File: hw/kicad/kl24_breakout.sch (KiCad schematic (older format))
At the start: 21 parts

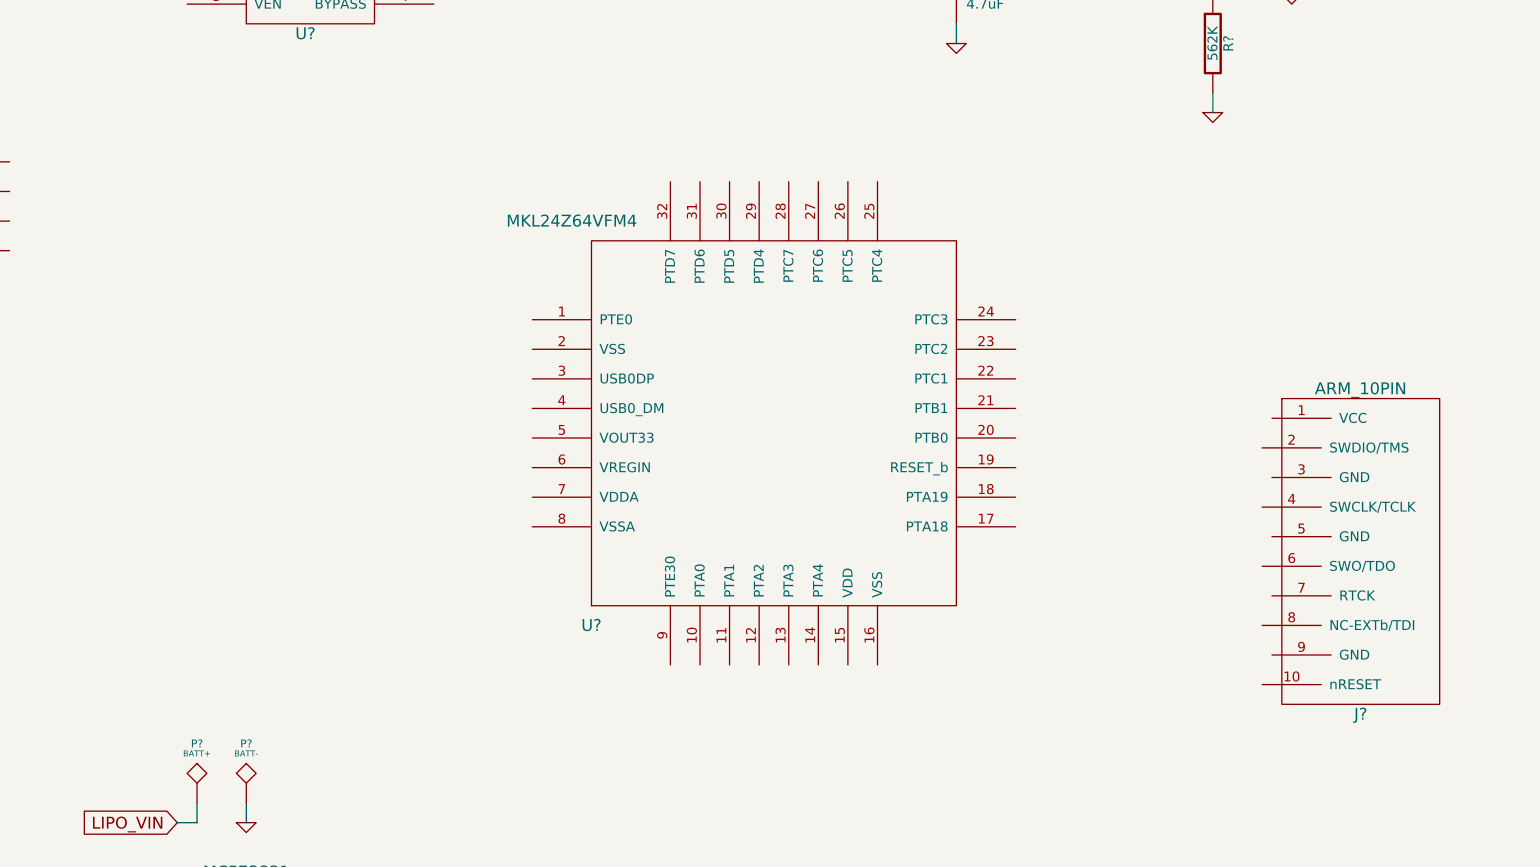
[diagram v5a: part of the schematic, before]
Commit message: - add some usb things and a crystal+load caps
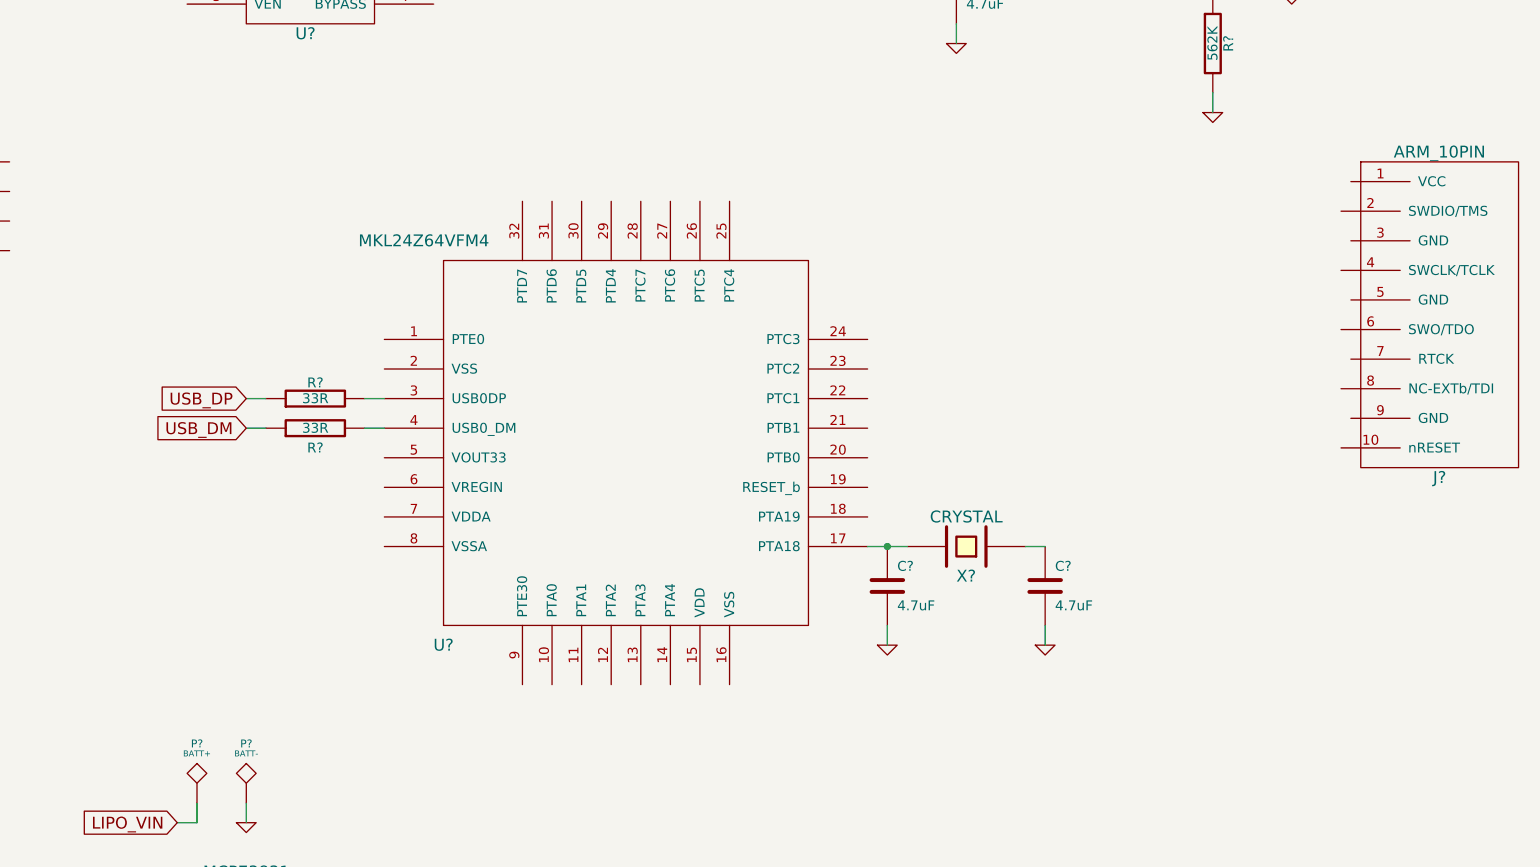
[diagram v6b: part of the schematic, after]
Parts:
- added C? (x2): 4.7uF, symbol C
- added R? (x2): 33R, symbol R
- added X?: CRYSTAL, ~, symbol CRYSTAL
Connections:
- net GND: now also C?.2, C?.2
- net USB_DM: now also R?.1
- net USB_DP: now also R?.1
- net at U?.17 (PTA18): now also C?.1, X?.2
- net at U?.3 (USB0DP): now also R?.2
- net at U?.4 (USB0_DM): now also R?.2
- new net: C?.1, X?.1
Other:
- moved on the sheet: J?, U?
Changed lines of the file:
@@
-EESchema Schematic File Version 2  date 3/9/2013 12:31:52 PM
+EESchema Schematic File Version 2  date 3/9/2013 4:44:26 PM
 LIBS:power
 LIBS:device
@@
 LIBS:kl24_breakout
 LIBS:kl24_breakout-cache
-EELAYER 25  0
+EELAYER 27 0
 EELAYER END
-$Descr A4 11700 8267
+$Descr A4 11693 8268
 encoding utf-8
 Sheet 1 1
@@
 F 0 "#PWR?" H 5700 6950 30  0001 C CNN
 F 1 "GND" H 5700 6880 30  0001 C CNN
+F 2 "" H 5700 6950 60  0001 C CNN
+F 3 "" H 5700 6950 60  0001 C CNN
 	1    5700 6950
 	1    0    0    -1
@@
 F 0 "C?" H 5750 6750 50  0000 L CNN
 F 1 "4.7uF" H 5750 6550 50  0000 L CNN
+F 2 "" H 5700 6650 60  0001 C CNN
+F 3 "" H 5700 6650 60  0001 C CNN
 	1    5700 6650
 	1    0    0    -1
@@
 F 0 "R?" V 5530 6850 50  0000 C CNN
 F 1 "2K" V 5450 6850 50  0000 C CNN
+F 2 "" H 5450 6850 60  0001 C CNN
+F 3 "" H 5450 6850 60  0001 C CNN
 	1    5450 6850
 	1    0    0    -1
@@
 F 0 "R?" V 3780 7200 50  0000 C CNN
 F 1 "470R" V 3700 7200 50  0000 C CNN
+F 2 "" H 3700 7200 60  0001 C CNN
+F 3 "" H 3700 7200 60  0001 C CNN
 	1    3700 7200
 	1    0    0    -1
@@
 F 0 "D?" H 3700 6750 50  0000 C CNN
 F 1 "LED" H 3700 6550 50  0000 C CNN
+F 2 "" H 3700 6650 60  0001 C CNN
+F 3 "" H 3700 6650 60  0001 C CNN
 	1    3700 6650
 	0    1    1    0
@@
 F 0 "#PWR?" H 3300 6950 30  0001 C CNN
 F 1 "GND" H 3300 6880 30  0001 C CNN
+F 2 "" H 3300 6950 60  0001 C CNN
+F 3 "" H 3300 6950 60  0001 C CNN
 	1    3300 6950
 	1    0    0    -1
@@
 F 0 "C?" H 3200 6750 50  0000 L CNN
 F 1 "4.7uF" H 3100 6550 50  0000 L CNN
+F 2 "" H 3300 6650 60  0001 C CNN
+F 3 "" H 3300 6650 60  0001 C CNN
 	1    3300 6650
 	1    0    0    -1
@@
 F 0 "#PWR?" H 5150 6850 30  0001 C CNN
 F 1 "GND" H 5150 6780 30  0001 C CNN
+F 2 "" H 5150 6850 60  0001 C CNN
+F 3 "" H 5150 6850 60  0001 C CNN
 	1    5150 6850
 	1    0    0    -1
@@
 F 0 "L?" V 7750 1200 40  0000 C CNN
 F 1 "INDUCTOR" V 7900 1200 40  0000 C CNN
+F 2 "" H 7800 1200 60  0001 C CNN
+F 3 "" H 7800 1200 60  0001 C CNN
 	1    7800 1200
 	0    -1   -1   0
@@
 F 0 "#PWR?" H 9800 1850 30  0001 C CNN
 F 1 "GND" H 9800 1780 30  0001 C CNN
+F 2 "" H 9800 1850 60  0001 C CNN
+F 3 "" H 9800 1850 60  0001 C CNN
 	1    9800 1850
 	1    0    0    -1
@@
 F 0 "C?" H 9850 1650 50  0000 L CNN
 F 1 "10uF" H 9850 1450 50  0000 L CNN
+F 2 "" H 9800 1550 60  0001 C CNN
+F 3 "" H 9800 1550 60  0001 C CNN
 	1    9800 1550
 	1    0    0    -1
@@
 F 0 "#PWR?" H 9400 2450 30  0001 C CNN
 F 1 "GND" H 9400 2380 30  0001 C CNN
+F 2 "" H 9400 2450 60  0001 C CNN
+F 3 "" H 9400 2450 60  0001 C CNN
 	1    9400 2450
 	1    0    0    -1
@@
 F 0 "R?" V 9480 2100 50  0000 C CNN
 F 1 "562K" V 9400 2100 50  0000 C CNN
+F 2 "" H 9400 2100 60  0001 C CNN
+F 3 "" H 9400 2100 60  0001 C CNN
 	1    9400 2100
 	1    0    0    -1
@@
 F 0 "R?" V 9630 1600 50  0000 C CNN
 F 1 "976K" V 9550 1600 50  0000 C CNN
+F 2 "" H 9550 1600 60  0001 C CNN
+F 3 "" H 9550 1600 60  0001 C CNN
 	1    9550 1600
 	1    0    0    -1
@@
 F 0 "#PWR?" H 8100 1350 30  0001 C CNN
 F 1 "GND" H 8100 1280 30  0001 C CNN
+F 2 "" H 8100 1350 60  0001 C CNN
+F 3 "" H 8100 1350 60  0001 C CNN
 	1    8100 1350
 	1    0    0    -1
@@
 F 0 "#PWR?" H 8100 2100 30  0001 C CNN
 F 1 "GND" H 8100 2030 30  0001 C CNN
+F 2 "" H 8100 2100 60  0001 C CNN
+F 3 "" H 8100 2100 60  0001 C CNN
 	1    8100 2100
 	1    0    0    -1
@@
 F 0 "C?" H 8150 1900 50  0000 L CNN
 F 1 "4.7uF" H 8150 1700 50  0000 L CNN
+F 2 "" H 8100 1800 60  0001 C CNN
+F 3 "" H 8100 1800 60  0001 C CNN
 	1    8100 1800
 	1    0    0    -1
@@
 F 0 "#PWR?" H 2350 5450 30  0001 C CNN
 F 1 "GND" H 2350 5380 30  0001 C CNN
+F 2 "" H 2350 5450 60  0001 C CNN
+F 3 "" H 2350 5450 60  0001 C CNN
 	1    2350 5450
 	1    0    0    -1
@@
 F 0 "#PWR?" H 4500 6050 30  0001 C CNN
 F 1 "GND" H 4500 5980 30  0001 C CNN
+F 2 "" H 4500 6050 60  0001 C CNN
+F 3 "" H 4500 6050 60  0001 C CNN
 	1    4500 6050
 	1    0    0    -1
@@
 F 0 "#PWR?" H 9800 950 30  0001 C CNN
 F 1 "GND" H 9800 880 30  0001 C CNN
+F 2 "" H 9800 950 60  0001 C CNN
+F 3 "" H 9800 950 60  0001 C CNN
 	1    9800 950
 	1    0    0    -1
@@
 F 0 "P?" H 9800 1150 40  0000 C CNN
 F 1 "BATT_BACKUP-" H 9800 1100 30  0000 C CNN
+F 2 "" H 9800 850 60  0001 C CNN
+F 3 "" H 9800 850 60  0001 C CNN
 	1    9800 850
 	1    0    0    -1
@@
 F 0 "P?" H 9400 1400 40  0000 C CNN
 F 1 "BATT_BACKUP+" H 9400 1350 30  0000 C CNN
+F 2 "" H 9400 1100 60  0001 C CNN
+F 3 "" H 9400 1100 60  0001 C CNN
 	1    9400 1100
 	1    0    0    -1
@@
 F 0 "U?" H 8750 1050 60  0000 C CNN
 F 1 "MCP1640_SOT23" H 8750 1650 60  0000 C CNN
+F 2 "" H 8750 1350 60  0001 C CNN
+F 3 "" H 8750 1350 60  0001 C CNN
 	1    8750 1350
 	1    0    0    -1
@@
 F 0 "U?" H 4500 6300 60  0000 C CNN
 F 1 "MCP73831" H 4500 6900 60  0000 C CNN
+F 2 "" H 4500 6600 60  0001 C CNN
+F 3 "" H 4500 6600 60  0001 C CNN
 	1    4500 6600
 	1    0    0    -1
@@
 F 0 "U?" H 2600 2600 60  0000 C CNN
 F 1 "MCP1252-33X50I" H 2600 3350 60  0000 C CNN
+F 2 "" H 2600 2950 60  0001 C CNN
+F 3 "" H 2600 2950 60  0001 C CNN
 	1    2600 2950
 	1    0    0    -1
@@
 F 0 "U?" H 4800 1450 60  0000 C CNN
 F 1 "LP3985" H 4850 2050 60  0000 C CNN
+F 2 "" H 4800 1750 60  0001 C CNN
+F 3 "" H 4800 1750 60  0001 C CNN
 	1    4800 1750
 	1    0    0    -1
@@
 L ARM_10PIN J?
 U 1 1 51353F09
-P 10150 4500
-F 0 "J?" H 10150 3500 60  0000 C CNN
-F 1 "ARM_10PIN" H 10150 5150 60  0000 C CNN
-	1    10150 4500
+P 10550 3300
+F 0 "J?" H 10550 2300 60  0000 C CNN
+F 1 "ARM_10PIN" H 10550 3950 60  0000 C CNN
+F 2 "" H 10550 3300 60  0001 C CNN
+F 3 "" H 10550 3300 60  0001 C CNN
+	1    10550 3300
 	-1   0    0    -1
 $EndComp
@@
 F 0 "P?" H 4500 6250 40  0000 C CNN
 F 1 "BATT-" H 4500 6200 30  0000 C CNN
+F 2 "" H 4500 5950 60  0001 C CNN
+F 3 "" H 4500 5950 60  0001 C CNN
 	1    4500 5950
 	1    0    0    -1
@@
 F 0 "P?" H 4250 6250 40  0000 C CNN
 F 1 "BATT+" H 4250 6200 30  0000 C CNN
+F 2 "" H 4250 5950 60  0001 C CNN
+F 3 "" H 4250 5950 60  0001 C CNN
 	1    4250 5950
 	1    0    0    -1
@@
 F 0 "J?" H 1950 4400 60  0000 C CNN
 F 1 "USB-micro-ab" H 1950 5650 60  0000 C CNN
+F 2 "" H 1950 5000 60  0001 C CNN
+F 3 "" H 1950 5000 60  0001 C CNN
 	1    1950 5000
 	1    0    0    -1
@@
 L MKL24Z64VFM4 U?
 U 1 1 512F925B
-P 6650 4400
-F 0 "U?" H 6250 3750 60  0000 C CNN
-F 1 "MKL24Z64VFM4" H 6150 5800 60  0000 C CNN
-	1    6650 4400
-	1    0    0    -1
-$EndComp
+P 5900 4500
+F 0 "U?" H 5500 3850 60  0000 C CNN
+F 1 "MKL24Z64VFM4" H 5400 5900 60  0000 C CNN
+F 2 "" H 5900 4500 60  0001 C CNN
+F 3 "" H 5900 4500 60  0001 C CNN
+	1    5900 4500
+	1    0    0    -1
+$EndComp
+$Comp
+L CRYSTAL X?
+U 1 1 513BACD6
+P 8150 4650
+F 0 "X?" H 8150 4800 60  0000 C CNN
+F 1 "CRYSTAL" H 8150 4500 60  0000 C CNN
+F 2 "~" H 8150 4650 60  0000 C CNN
+F 3 "~" H 8150 4650 60  0000 C CNN
+	1    8150 4650
+	-1   0    0    1
+$EndComp
+$Comp
+L C C?
+U 1 1 513BAD01
+P 7750 4850
+F 0 "C?" H 7800 4950 50  0000 L CNN
+F 1 "4.7uF" H 7800 4750 50  0000 L CNN
+F 2 "" H 7750 4850 60  0001 C CNN
+F 3 "" H 7750 4850 60  0001 C CNN
+	1    7750 4850
+	1    0    0    -1
+$EndComp
+$Comp
+L C C?
+U 1 1 513BAD11
+P 8550 4850
+F 0 "C?" H 8600 4950 50  0000 L CNN
+F 1 "4.7uF" H 8600 4750 50  0000 L CNN
+F 2 "" H 8550 4850 60  0001 C CNN
+F 3 "" H 8550 4850 60  0001 C CNN
+	1    8550 4850
+	1    0    0    -1
+$EndComp
+$Comp
+L GND #PWR?
+U 1 1 513BAD17
+P 7750 5150
+F 0 "#PWR?" H 7750 5150 30  0001 C CNN
+F 1 "GND" H 7750 5080 30  0001 C CNN
+F 2 "" H 7750 5150 60  0001 C CNN
+F 3 "" H 7750 5150 60  0001 C CNN
+	1    7750 5150
+	1    0    0    -1
+$EndComp
+$Comp
+L GND #PWR?
+U 1 1 513BAD27
+P 8550 5150
+F 0 "#PWR?" H 8550 5150 30  0001 C CNN
+F 1 "GND" H 8550 5080 30  0001 C CNN
+F 2 "" H 8550 5150 60  0001 C CNN
+F 3 "" H 8550 5150 60  0001 C CNN
+	1    8550 5150
+	1    0    0    -1
+$EndComp
+Wire Wire Line
+	8550 5050 8550 5150
+Wire Wire Line
+	7750 5050 7750 5150
+Wire Wire Line
+	7650 4650 7850 4650
+Connection ~ 7750 4650
+Wire Wire Line
+	8450 4650 8550 4650
+Text GLabel 4500 4050 0    60   Input ~ 0
+USB_DM
+$Comp
+L R R?
+U 1 1 513BAF17
+P 4850 4050
+F 0 "R?" V 4750 4050 50  0000 C CNN
+F 1 "33R" V 4850 4050 50  0000 C CNN
+F 2 "" H 4850 4050 60  0001 C CNN
+F 3 "" H 4850 4050 60  0001 C CNN
+	1    4850 4050
+	0    -1   -1   0
+$EndComp
+Wire Wire Line
+	4500 4050 4600 4050
+Wire Wire Line
+	5100 4050 5200 4050
+Text GLabel 4500 3900 0    60   Input ~ 0
+USB_DP
+$Comp
+L R R?
+U 1 1 513BB078
+P 4850 3900
+F 0 "R?" V 4930 3900 50  0000 C CNN
+F 1 "33R" V 4850 3900 50  0000 C CNN
+F 2 "" H 4850 3900 60  0001 C CNN
+F 3 "" H 4850 3900 60  0001 C CNN
+	1    4850 3900
+	0    -1   -1   0
+$EndComp
+Wire Wire Line
+	5100 3900 5200 3900
+Wire Wire Line
+	4600 3900 4500 3900
 $EndSCHEMATC

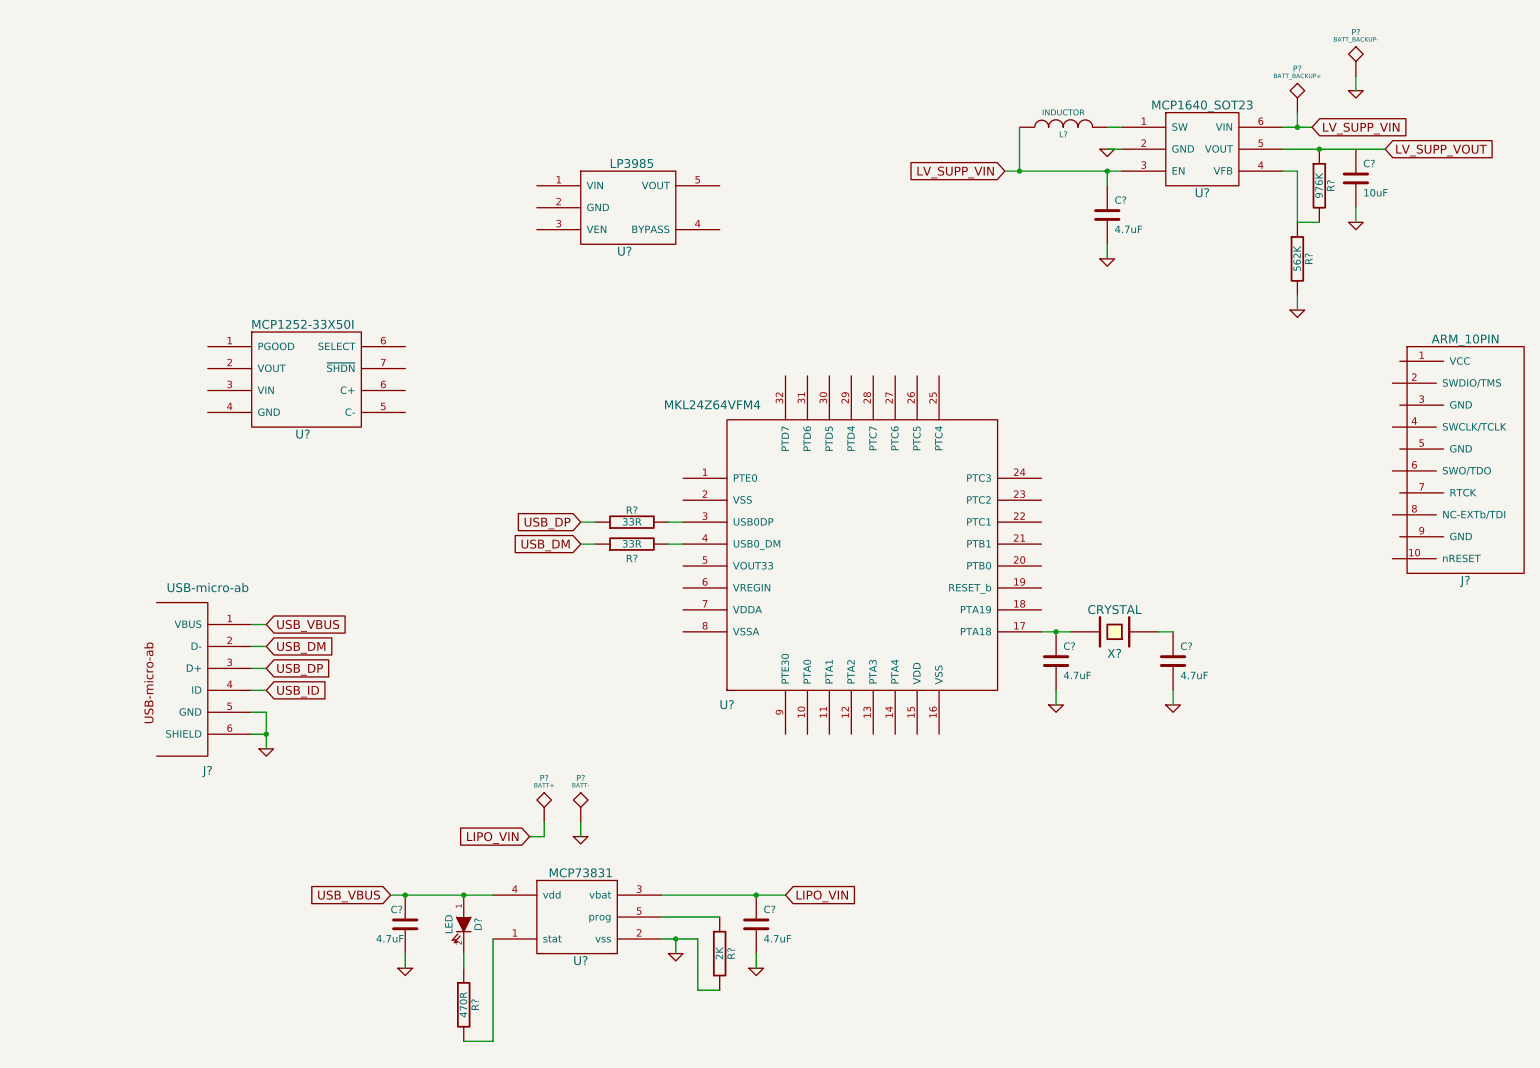
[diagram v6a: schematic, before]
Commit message: - add global labels to all pins for breaking out to test pads.
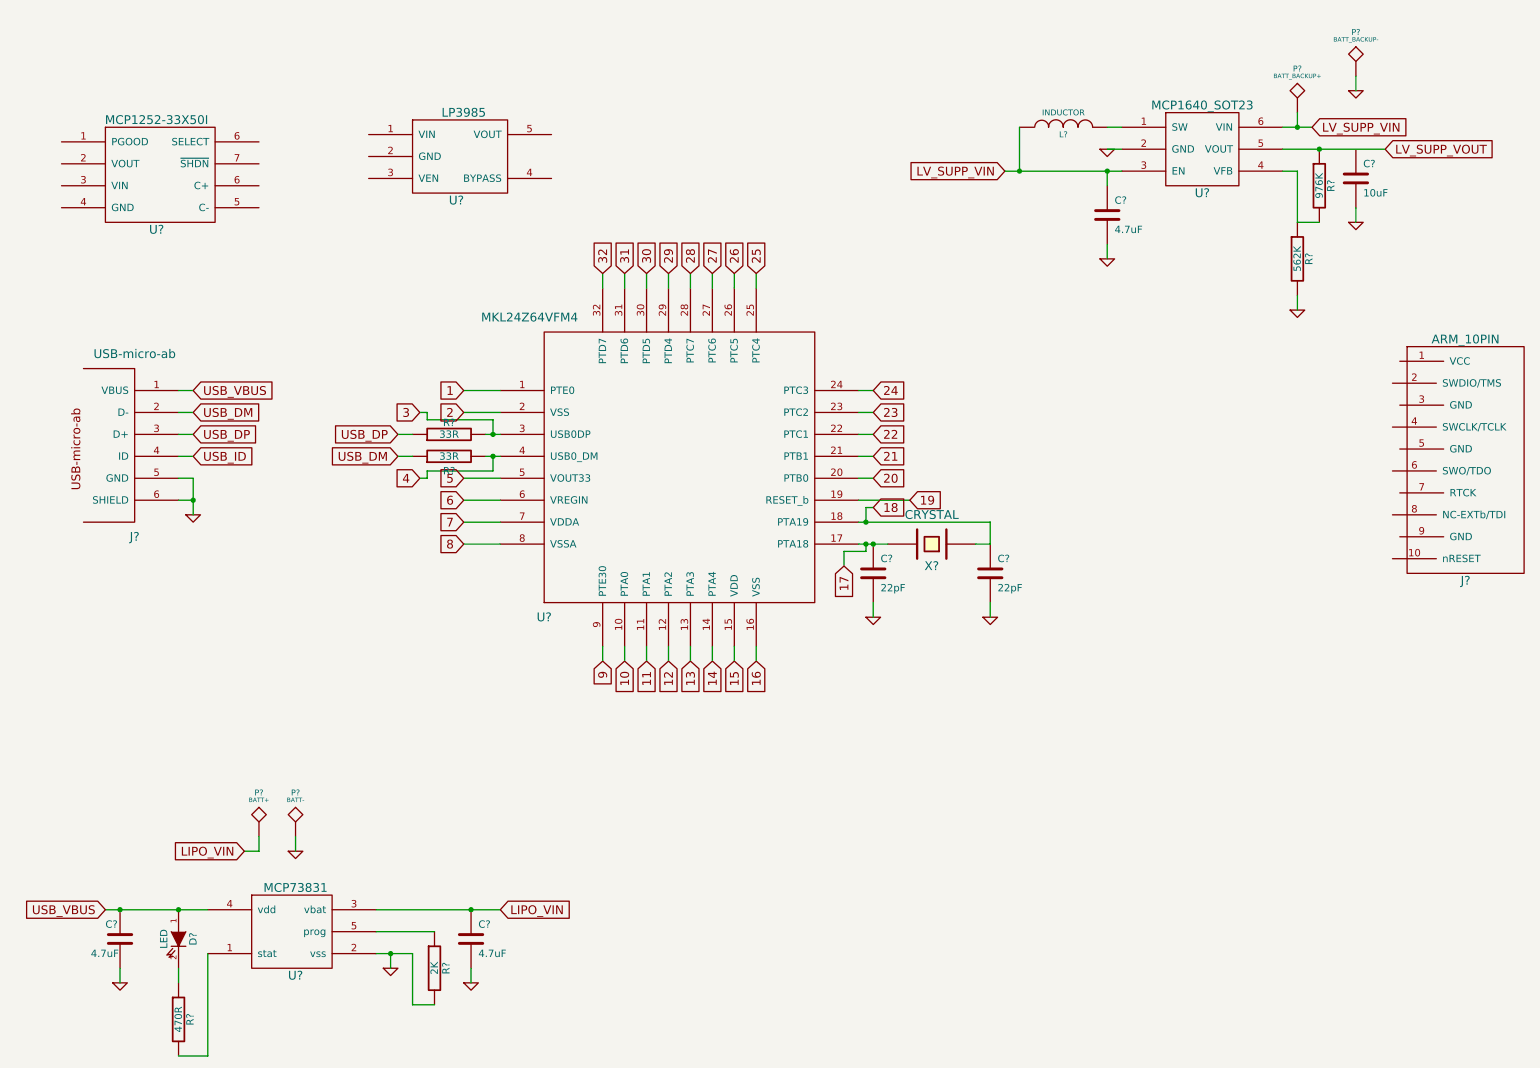
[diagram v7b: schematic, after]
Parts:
- C? (x2): value 4.7uF -> 22pF
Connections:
- net 1: now reaches U?.1 (PTE0)
- net 10: now reaches U?.10 (PTA0)
- net 11: now reaches U?.11 (PTA1)
- net 12: now reaches U?.12 (PTA2)
- net 13: now reaches U?.13 (PTA3)
- net 14: now reaches U?.14 (PTA4)
- net 15: now reaches U?.15 (VDD)
- net 16: now reaches U?.16 (VSS)
- net 17: now reaches C?.1, U?.17 (PTA18), X?.2
- net 18: now reaches U?.18 (PTA19)
- net 18: now also C?.1, X?.1
- net 19: now reaches U?.19 (RESET_b)
- net 2: now reaches U?.2 (VSS)
- net 20: now reaches U?.20 (PTB0)
- net 21: now reaches U?.21 (PTB1)
- net 22: now reaches U?.22 (PTC1)
- net 23: now reaches U?.23 (PTC2)
- net 24: now reaches U?.24 (PTC3)
- net 25: now reaches U?.25 (PTC4)
- net 26: now reaches U?.26 (PTC5)
- net 27: now reaches U?.27 (PTC6)
- net 28: now reaches U?.28 (PTC7)
- net 29: now reaches U?.29 (PTD4)
- net 3: now reaches R?.2, U?.3 (USB0DP)
- net 30: now reaches U?.30 (PTD5)
- net 31: now reaches U?.31 (PTD6)
- net 32: now reaches U?.32 (PTD7)
- net 4: now reaches R?.2, U?.4 (USB0_DM)
- net 5: now reaches U?.5 (VOUT33)
- net 6: now reaches U?.6 (VREGIN)
- net 7: now reaches U?.7 (VDDA)
- net 8: now reaches U?.8 (VSSA)
- net 9: now reaches U?.9 (PTE30)
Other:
- moved on the sheet: C?, D?, J?, P?, R?, U?, X?
